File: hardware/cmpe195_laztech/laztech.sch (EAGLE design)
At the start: 28 parts

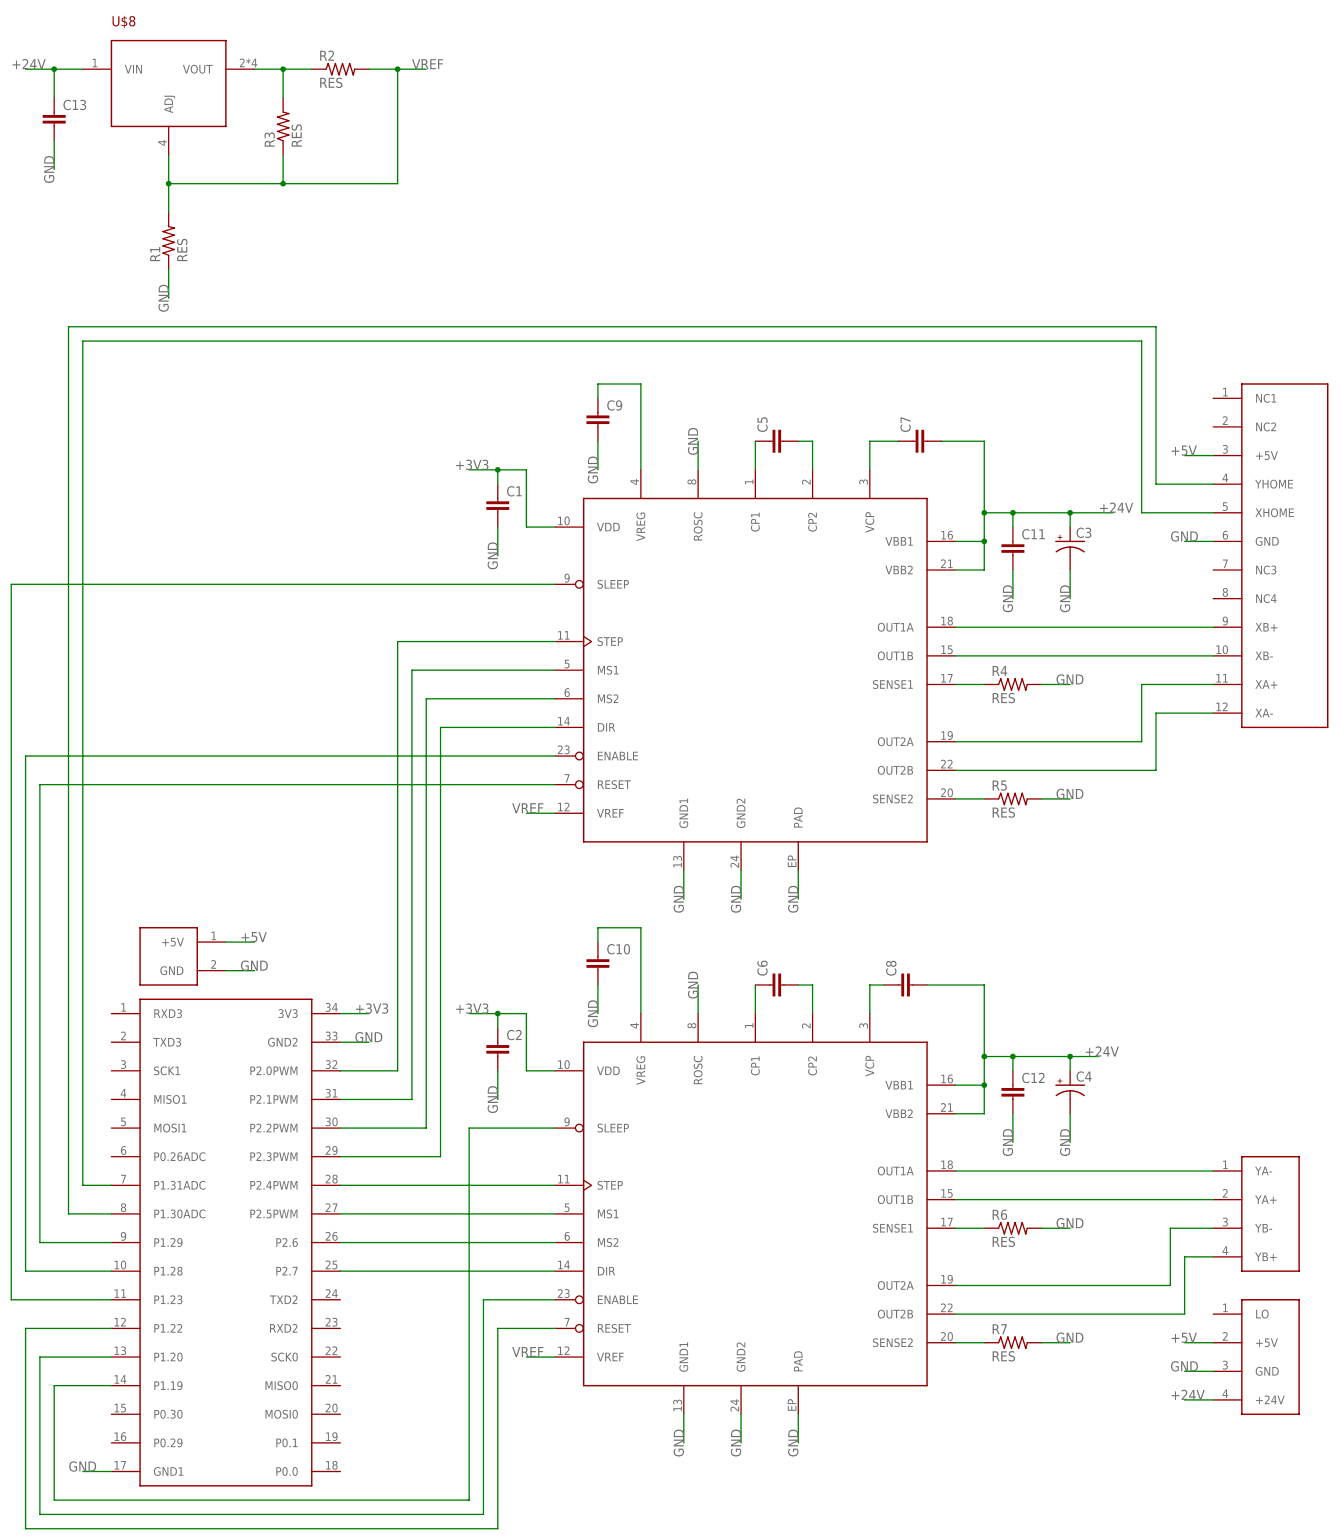
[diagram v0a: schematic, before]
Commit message: Added resistor packages.
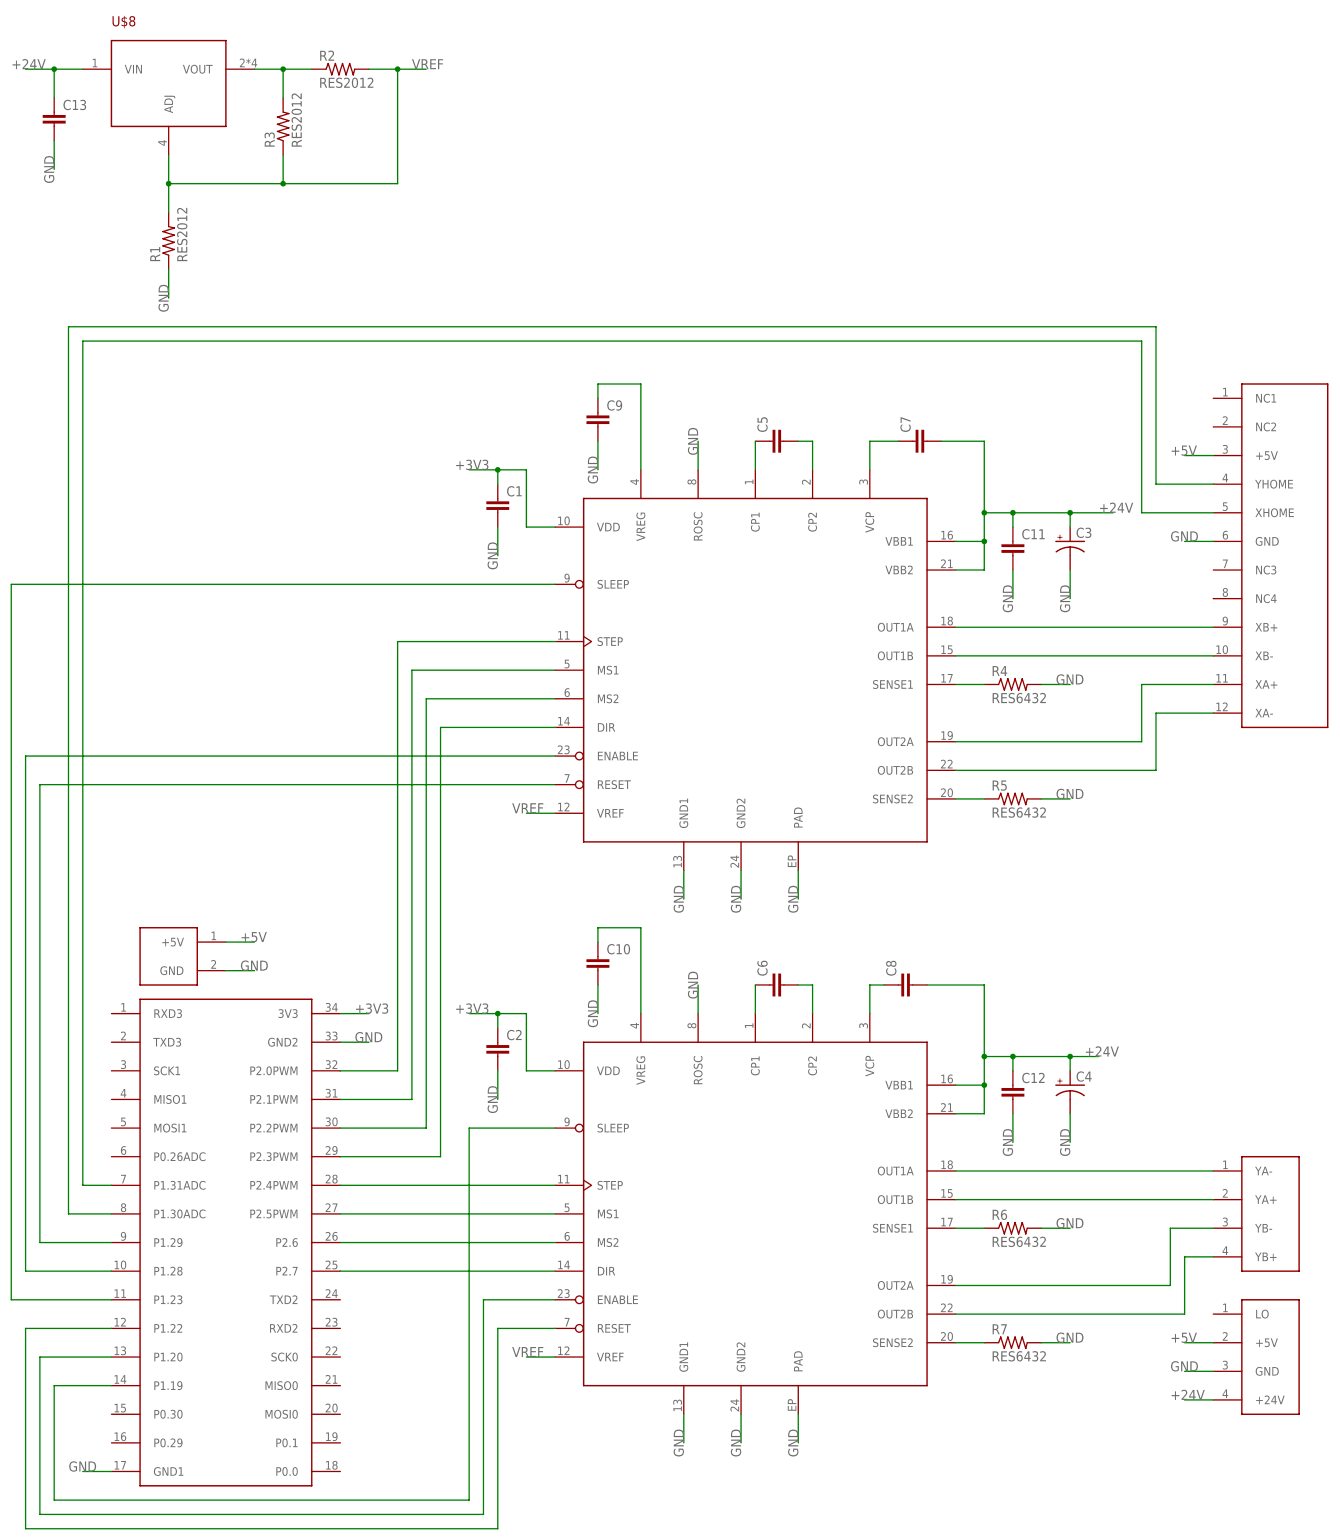
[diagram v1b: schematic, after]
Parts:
- R1, R2, R3: value RES -> RES2012; device laztech_parts:RES -> laztech_parts:RES2012
- R4, R5, R6, R7: value RES -> RES6432; device laztech_parts:RES -> laztech_parts:RES6432
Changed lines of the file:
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@@
 <part name="U$8" library="laztech_parts" deviceset="LM317" device=""/>
 <part name="C13" library="laztech_parts" deviceset="CAP" device=""/>
-<part name="R1" library="laztech_parts" deviceset="RES" device=""/>
-<part name="R2" library="laztech_parts" deviceset="RES" device=""/>
-<part name="R3" library="laztech_parts" deviceset="RES" device=""/>
-<part name="R4" library="laztech_parts" deviceset="RES" device=""/>
-<part name="R5" library="laztech_parts" deviceset="RES" device=""/>
-<part name="R6" library="laztech_parts" deviceset="RES" device=""/>
-<part name="R7" library="laztech_parts" deviceset="RES" device=""/>
+<part name="R1" library="laztech_parts" deviceset="RES" device="2012" value="RES2012"/>
+<part name="R2" library="laztech_parts" deviceset="RES" device="2012" value="RES2012"/>
+<part name="R3" library="laztech_parts" deviceset="RES" device="2012" value="RES2012"/>
+<part name="R4" library="laztech_parts" deviceset="RES" device="6432" value="RES6432"/>
+<part name="R5" library="laztech_parts" deviceset="RES" device="6432" value="RES6432"/>
+<part name="R6" library="laztech_parts" deviceset="RES" device="6432" value="RES6432"/>
+<part name="R7" library="laztech_parts" deviceset="RES" device="6432" value="RES6432"/>
 </parts>
 <sheets>

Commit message: Pre-route checkpoint.
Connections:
- net N$1: now also U$5.XB-; no longer U$5.XB+
- net N$2: now also U$5.XB+; no longer U$5.XB-
- net N$5: now also U$2.OUT1B; no longer U$2.OUT1A
- net N$6: now also U$2.OUT1A; no longer U$2.OUT1B
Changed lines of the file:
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@@
 </busses>
 <nets>
-<net name="N$5" class="0">
-<segment>
-<pinref part="U$2" gate="G$1" pin="OUT1A"/>
-<wire x1="259.08" y1="68.58" x2="304.8" y2="68.58" width="0.1524" layer="91"/>
-<pinref part="U$6" gate="G$1" pin="YA-"/>
-</segment>
-</net>
-<net name="N$6" class="0">
-<segment>
-<pinref part="U$2" gate="G$1" pin="OUT1B"/>
-<wire x1="259.08" y1="63.5" x2="304.8" y2="63.5" width="0.1524" layer="91"/>
-<pinref part="U$6" gate="G$1" pin="YA+"/>
-</segment>
-</net>
 <net name="N$7" class="0">
 <segment>
@@
 <wire x1="304.8" y1="195.58" x2="299.72" y2="195.58" width="0.1524" layer="91"/>
 <label x="297.18" y="195.58" size="1.778" layer="95"/>
-</segment>
-</net>
-<net name="N$1" class="0">
-<segment>
-<pinref part="U$1" gate="G$1" pin="OUT1A"/>
-<pinref part="U$5" gate="G$1" pin="XB+"/>
-<wire x1="259.08" y1="165.1" x2="304.8" y2="165.1" width="0.1524" layer="91"/>
-</segment>
-</net>
-<net name="N$2" class="0">
-<segment>
-<pinref part="U$1" gate="G$1" pin="OUT1B"/>
-<pinref part="U$5" gate="G$1" pin="XB-"/>
-<wire x1="259.08" y1="160.02" x2="304.8" y2="160.02" width="0.1524" layer="91"/>
 </segment>
 </net>
@@
 </segment>
 </net>
+<net name="N$5" class="0">
+<segment>
+<pinref part="U$2" gate="G$1" pin="OUT1B"/>
+<wire x1="259.08" y1="63.5" x2="294.64" y2="63.5" width="0.1524" layer="91"/>
+<wire x1="294.64" y1="63.5" x2="299.72" y2="68.58" width="0.1524" layer="91"/>
+<pinref part="U$6" gate="G$1" pin="YA-"/>
+<wire x1="299.72" y1="68.58" x2="304.8" y2="68.58" width="0.1524" layer="91"/>
+</segment>
+</net>
+<net name="N$6" class="0">
+<segment>
+<pinref part="U$2" gate="G$1" pin="OUT1A"/>
+<wire x1="259.08" y1="68.58" x2="294.64" y2="68.58" width="0.1524" layer="91"/>
+<wire x1="294.64" y1="68.58" x2="299.72" y2="63.5" width="0.1524" layer="91"/>
+<pinref part="U$6" gate="G$1" pin="YA+"/>
+<wire x1="299.72" y1="63.5" x2="304.8" y2="63.5" width="0.1524" layer="91"/>
+</segment>
+</net>
+<net name="N$1" class="0">
+<segment>
+<pinref part="U$1" gate="G$1" pin="OUT1A"/>
+<wire x1="259.08" y1="165.1" x2="294.64" y2="165.1" width="0.1524" layer="91"/>
+<wire x1="294.64" y1="165.1" x2="299.72" y2="160.02" width="0.1524" layer="91"/>
+<pinref part="U$5" gate="G$1" pin="XB-"/>
+<wire x1="299.72" y1="160.02" x2="304.8" y2="160.02" width="0.1524" layer="91"/>
+</segment>
+</net>
+<net name="N$2" class="0">
+<segment>
+<pinref part="U$1" gate="G$1" pin="OUT1B"/>
+<wire x1="259.08" y1="160.02" x2="294.64" y2="160.02" width="0.1524" layer="91"/>
+<wire x1="294.64" y1="160.02" x2="299.72" y2="165.1" width="0.1524" layer="91"/>
+<pinref part="U$5" gate="G$1" pin="XB+"/>
+<wire x1="299.72" y1="165.1" x2="304.8" y2="165.1" width="0.1524" layer="91"/>
+</segment>
+</net>

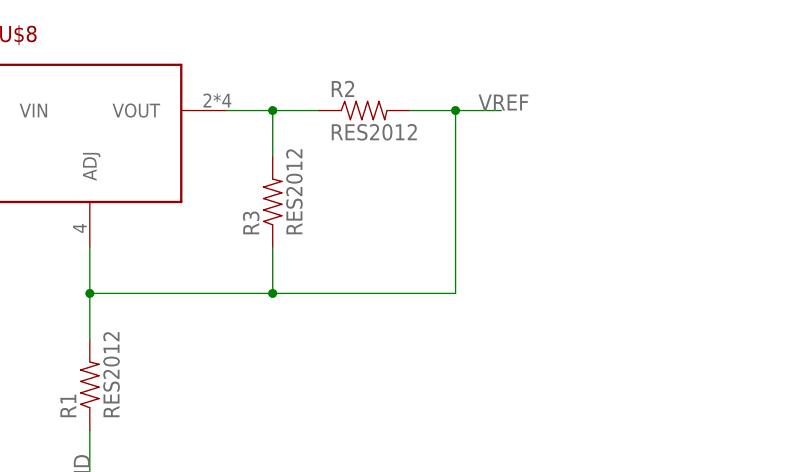
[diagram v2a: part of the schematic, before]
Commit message: Partial layout. Still need to route signals to uCPU.
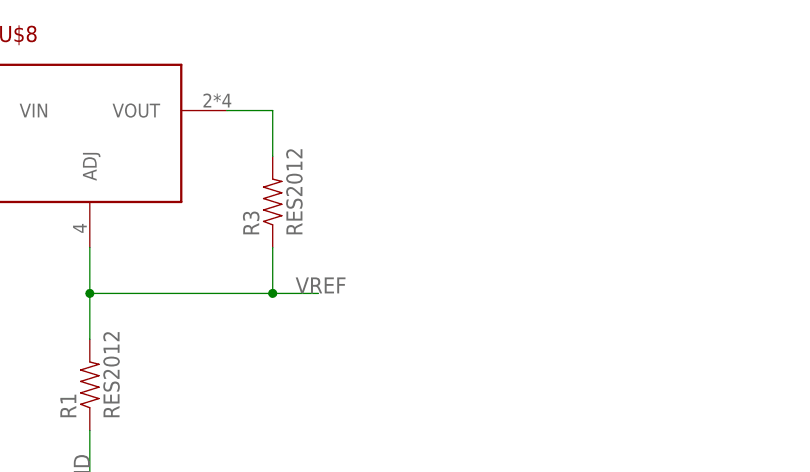
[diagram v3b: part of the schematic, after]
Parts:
- removed R2: RES2012, laztech_parts:RES2012
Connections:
- net N$34: no longer R2.1
- net VREF: no longer R2.2
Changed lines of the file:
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@@
 <part name="C13" library="laztech_parts" deviceset="CAP" device=""/>
 <part name="R1" library="laztech_parts" deviceset="RES" device="2012" value="RES2012"/>
-<part name="R2" library="laztech_parts" deviceset="RES" device="2012" value="RES2012"/>
 <part name="R3" library="laztech_parts" deviceset="RES" device="2012" value="RES2012"/>
 <part name="R4" library="laztech_parts" deviceset="RES" device="6432" value="RES6432"/>
@@
 <instance part="C13" gate="G$1" x="99.06" y="254"/>
 <instance part="R1" gate="G$1" x="119.38" y="233.68" rot="R90"/>
-<instance part="R2" gate="G$1" x="149.86" y="264.16"/>
 <instance part="R3" gate="G$1" x="139.7" y="254" rot="R90"/>
 <instance part="R4" gate="G$1" x="269.24" y="154.94"/>
@@
 <segment>
 <pinref part="U$8" gate="G$1" pin="VOUT"/>
-<pinref part="R2" gate="G$1" pin="1"/>
 <wire x1="134.62" y1="264.16" x2="139.7" y2="264.16" width="0.1524" layer="91"/>
 <pinref part="R3" gate="G$1" pin="2"/>
-<wire x1="139.7" y1="264.16" x2="144.78" y2="264.16" width="0.1524" layer="91"/>
 <wire x1="139.7" y1="259.08" x2="139.7" y2="264.16" width="0.1524" layer="91"/>
-<junction x="139.7" y="264.16"/>
 </segment>
 </net>
@@
 <wire x1="139.7" y1="243.84" x2="119.38" y2="243.84" width="0.1524" layer="91"/>
 <junction x="119.38" y="243.84"/>
-<pinref part="R2" gate="G$1" pin="2"/>
-<wire x1="154.94" y1="264.16" x2="160.02" y2="264.16" width="0.1524" layer="91"/>
-<wire x1="160.02" y1="264.16" x2="165.1" y2="264.16" width="0.1524" layer="91"/>
-<wire x1="139.7" y1="243.84" x2="160.02" y2="243.84" width="0.1524" layer="91"/>
-<wire x1="160.02" y1="243.84" x2="160.02" y2="264.16" width="0.1524" layer="91"/>
+<wire x1="139.7" y1="243.84" x2="144.78" y2="243.84" width="0.1524" layer="91"/>
 <junction x="139.7" y="243.84"/>
-<junction x="160.02" y="264.16"/>
-<label x="162.56" y="264.16" size="1.778" layer="95"/>
-</segment>
-<segment>
+<label x="142.24" y="243.84" size="1.778" layer="95"/>
+</segment>
+<segment>
